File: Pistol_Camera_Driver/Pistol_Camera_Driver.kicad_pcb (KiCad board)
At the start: 2 copper layers, 86.6 x 46.1 mm, 100 parts, among them J1 Screw_Terminal_01x02, J11 Screw_Terminal_01x02, J12 Screw_Terminal_01x02, J13 I2C, J14 Screw_Terminal_01x02, J15 Screw_Terminal_01x02, J16 Screw_Terminal_01x02, J17 Screw_Terminal_01x02, J18 Screw_Terminal_01x02, J19 I2C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

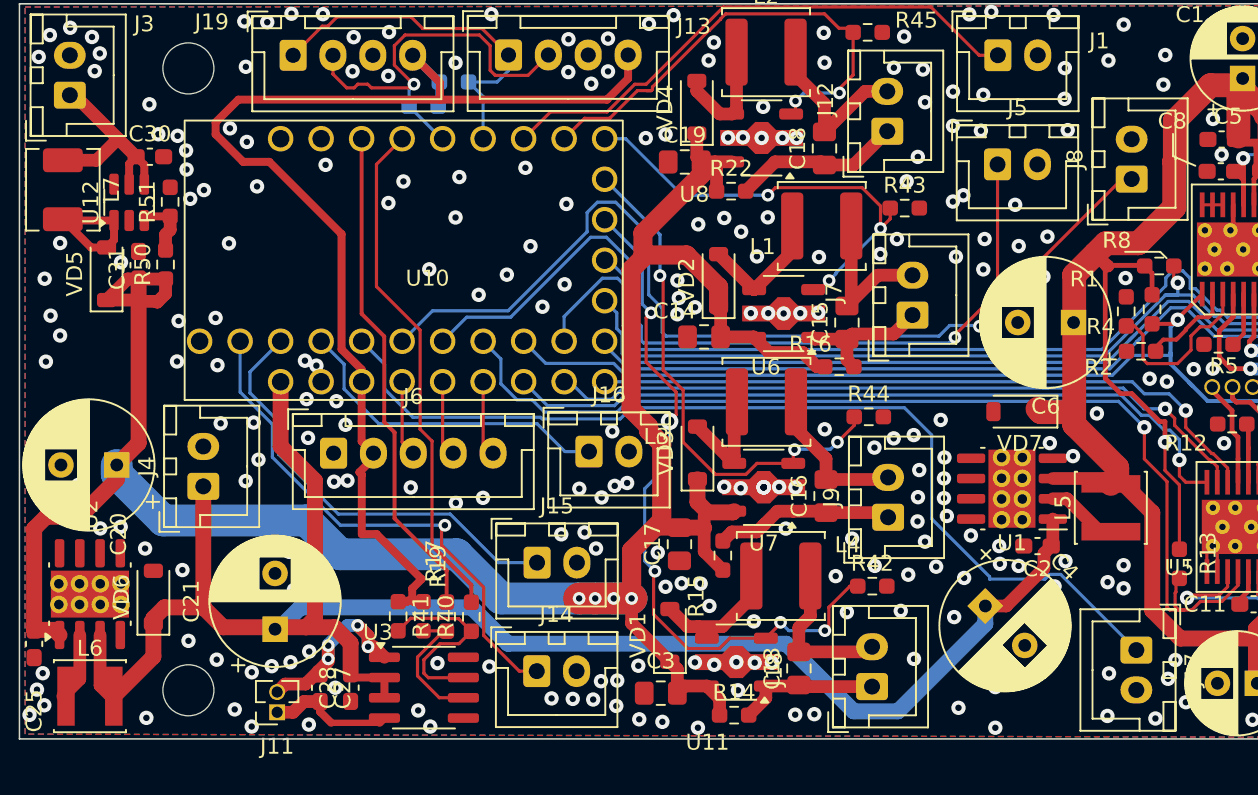
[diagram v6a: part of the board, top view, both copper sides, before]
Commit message: v0.8 compact BUCK converter for 3v3 was added
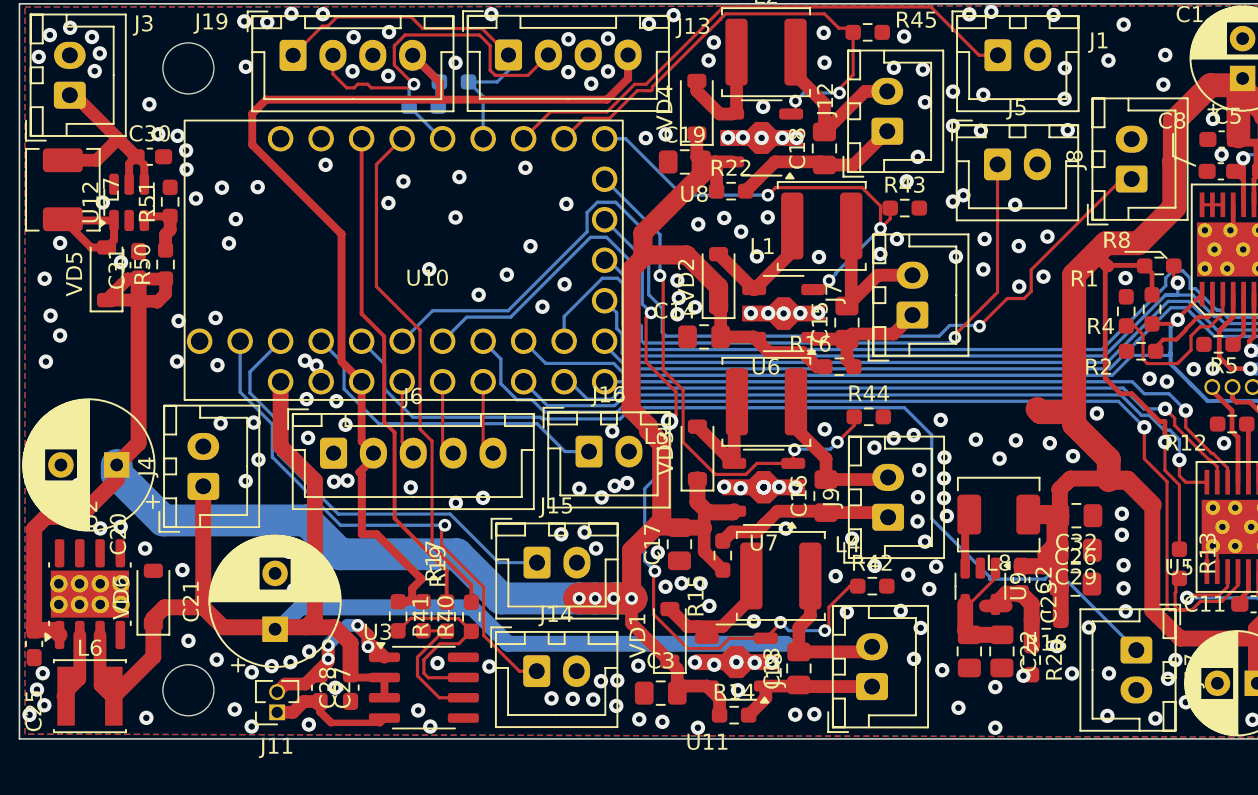
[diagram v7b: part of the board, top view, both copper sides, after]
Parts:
- removed C4: 470uF, Capacitor_THT:CP_Radial_D8.0mm_P3.50mm
- removed C6: 330uF, Capacitor_THT:CP_Radial_D8.0mm_P3.50mm
- removed L5: 22u, Inductor_SMD:L_Sunlord_SWPA4012S
- removed U1: XL1509-3.3, Package_SO:SOIC-8-1EP_3.9x4.9mm_P1.27mm_EP2.95x4.9mm_Mask2.71x3.4mm_ThermalVias
- removed VD7: CDBA3100-HF, Diode_SMD:D_SOD-123
- added C22: 22u, Capacitor_SMD:C_0805_2012Metric_Pad1.18x1.45mm_HandSolder, F.Cu at (91.7, 72.2)
- added C23: 22u, Capacitor_SMD:C_0805_2012Metric_Pad1.18x1.45mm_HandSolder, F.Cu at (89.6, 72.2)
- added C26: 22u, Capacitor_SMD:C_0805_2012Metric_Pad1.18x1.45mm_HandSolder, F.Cu at (96.3, 68.0)
- added C29: 22u, Capacitor_SMD:C_0805_2012Metric_Pad1.18x1.45mm_HandSolder, F.Cu at (96.3, 65.9)
- added C32: 22u, Capacitor_SMD:C_0805_2012Metric_Pad1.18x1.45mm_HandSolder, F.Cu at (96.3, 63.7)
- added L8: 4u7, Inductor_SMD:L_Chilisin_BMRx00040412, F.Cu at (91.5, 63.6)
- added R18: 45k, Resistor_SMD:R_0603_1608Metric_Pad0.98x0.95mm_HandSolder, F.Cu at (94.4, 70.3)
- added R20: 10k, Resistor_SMD:R_0603_1608Metric_Pad0.98x0.95mm_HandSolder, F.Cu at (93.5, 72.8)
- added U9: ~, Package_TO_SOT_SMD:SOT-23-5, F.Cu at (90.3, 68.1)
- C2: value 0.1 -> 1n
- R50: value R -> 100k
- R51: value R -> 10k
- moved C2 2.35 mm to (92.9, 67.7), turned to -90 degrees
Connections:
- C2 pad 1: +5V -> +3.3VP
- C2 pad 2: GND -> Net-(U9-FB)
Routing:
- net +5V: track 112.6 -> 87.0 mm
- net +3.3VP: track 117.0 -> 132.6 mm
- net VBUS: track 13.6 -> 20.7 mm
- net Net-(U9-FB): track 0.00 -> 6.74 mm
- net Net-(U1-OUT): track 4.49 -> 0.00 mm
- net +3V3: track 75.4 -> 71.5 mm
- net Net-(U9-SW): track 0.00 -> 3.47 mm

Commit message: v0.9 actual state
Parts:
- removed C20: 470uF, Capacitor_THT:CP_Radial_D8.0mm_P3.50mm
- removed C21: 330uF, Capacitor_THT:CP_Radial_D8.0mm_P3.50mm
- removed C25: 0.1, Capacitor_SMD:C_0603_1608Metric_Pad1.08x0.95mm_HandSolder
- removed L6: 22u, Inductor_SMD:L_Sunlord_SWPA4012S
- removed U2: XL1509-5.0, Package_SO:SOIC-8-1EP_3.9x4.9mm_P1.27mm_EP2.95x4.9mm_Mask2.71x3.4mm_ThermalVias
- removed VD6: CDBA3100-HF, Diode_SMD:D_SOD-123
- moved J3 31.2 mm to (40.8, 67.6), turned to 180 degrees
- moved L7 31.0 mm to (46.8, 71.0), turned to 0 degrees
- moved VD5 25.7 mm to (52.0, 68.2), turned to 180 degrees
- moved C30 25.2 mm to (44.7, 65.5), turned to 90 degrees
- moved U12 25.1 mm to (47.5, 66.8), turned to 180 degrees
- moved C31 23.0 mm to (51.5, 66.2), turned to 180 degrees
- moved R51 21.8 mm to (47.5, 64.2), turned to 180 degrees
- moved R50 20.6 mm to (51.4, 64.5), turned to 180 degrees
- moved J8 17.3 mm to (91.8, 57.9), turned to -90 degrees
- moved J2 5.39 mm to (108.4, 55.5)
- moved R41 4.77 mm to (54.1, 65.2)
- moved R40 4.77 mm to (55.7, 65.2)
- moved R17 4.77 mm to (57.2, 65.3)
- moved R19 4.77 mm to (58.7, 65.3)
- moved C26 4.11 mm to (96.6, 63.9)
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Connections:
- C28 pad 2: +5V -> +3.3VP
- J4 pad 1: +5V -> VBUS
- U10 pad 32: +5V -> VBUS
- U3 pad 2: +5V -> +3.3VP
- U3 pad 3: +5V -> +3.3VP
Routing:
- net +5V: track 87.0 -> 0.00 mm
- net VPP: track 153.1 -> 92.3 mm
- net (no net): track 0.00 -> 33.5 mm
- net +3.3VP: track 132.6 -> 100.3 mm
- net VBUS: track 20.7 -> 7.26 mm
- net Net-(U12-SW): track 8.60 -> 0.00 mm
- net +3V3: track 71.5 -> 63.9 mm
- net K2: track 61.5 -> 54.1 mm
- net MOTORS_nSLEEP: track 72.6 -> 66.9 mm
- net Net-(U5-CONFIG): track 17.6 -> 12.1 mm, vias 2 -> 1
- net GND: track 17.7 -> 23.3 mm, vias 285 -> 286
- net nFLT2: track 65.6 -> 60.7 mm
- net Net-(U9-FB): track 6.74 -> 1.88 mm
- net Net-(U2-OUT): track 4.28 -> 0.00 mm
- net nEN1: track 78.9 -> 74.9 mm
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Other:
- board size 86.6 x 46.1 mm -> 79.8 x 46.1 mm
